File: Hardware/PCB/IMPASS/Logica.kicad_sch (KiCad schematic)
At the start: 69 parts, among them J1 PUENTE H, J10 SENSORES, J12 POWER, J7 PUENTE H, J8 SOLENOIDES, J9 PROG, Q25 2N7002, Q26 2N7002, Q27 2N7002, Q28 2N7002, Q29 2N7002, Q30 2N7002, Q31 2N7002, Q32 2N7002, Q33 2N7002, Q34 2N7002, Q35 2N7002, Q36 2N7002, Q37 2N7002, Q38 2N7002, Q39 2N7002, Q40 2N7002, Q41 2N7002, Q42 2N7002, Q46 2N7002, Q47 2N7002, Q48 2N7002, SW1 RESET, SW2 BOOT, U1 ESP32-S3-WROOM-1, U10 AMS1117-3.3, U11 AMS1117-5.0

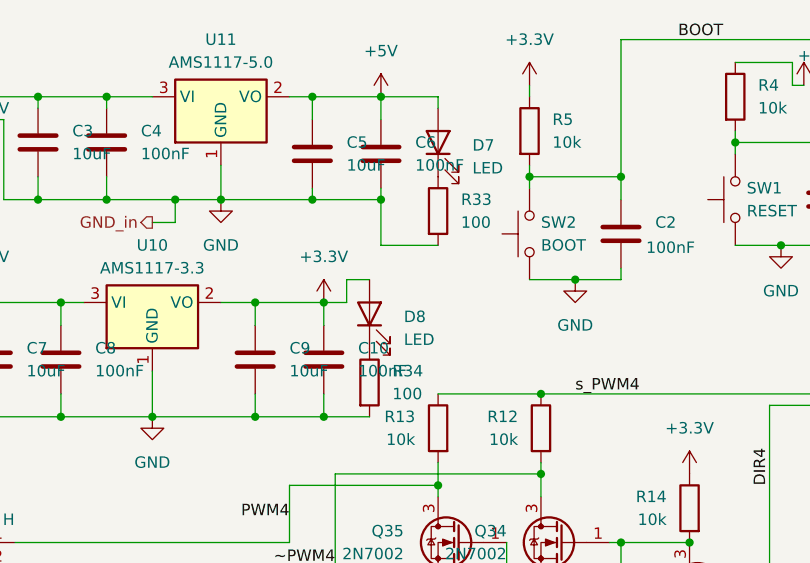
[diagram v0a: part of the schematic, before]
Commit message: Schematics: Added mpu6050
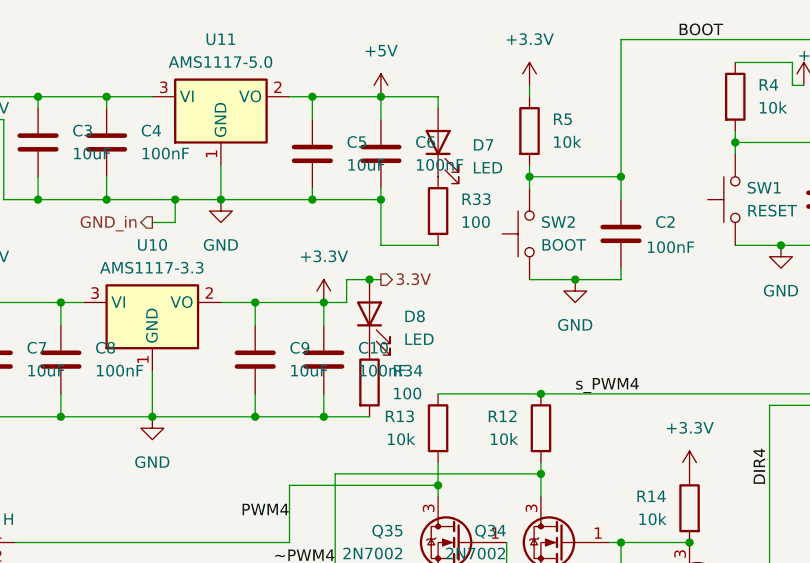
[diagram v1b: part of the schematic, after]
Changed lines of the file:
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@@
 	)
 	(junction
+		(at 63.5 40.64)
+		(diameter 0)
+		(color 0 0 0 0)
+	)
+	(junction
 		(at 204.47 73.66)
 		(diameter 0)
@@
 	(wire
 		(pts
+			(xy 63.5 40.64) (xy 64.77 40.64)
+		)
+		(stroke
+			(width 0)
+			(type default)
+		)
+	)
+	(wire
+		(pts
 			(xy 170.18 30.48) (xy 170.18 36.83)
 		)
@@
 		)
 	)
+	(hierarchical_label "3.3V"
+		(shape output)
+		(at 64.77 40.64 0)
+		(effects
+			(font
+				(size 1.27 1.27)
+			)
+			(justify left)
+		)
+	)

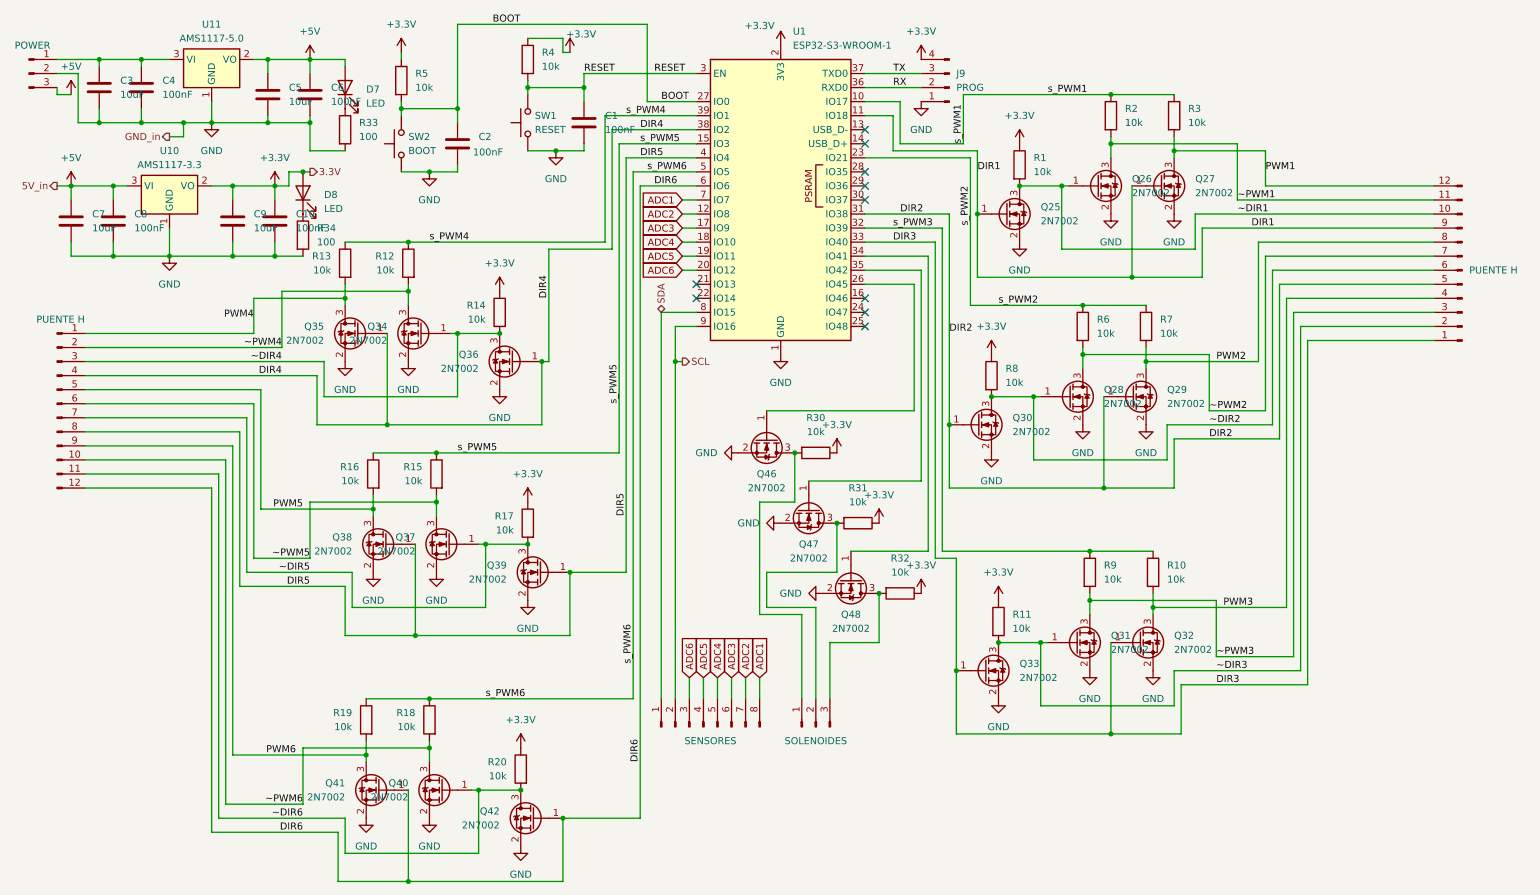
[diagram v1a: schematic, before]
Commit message: Restore all the schematics
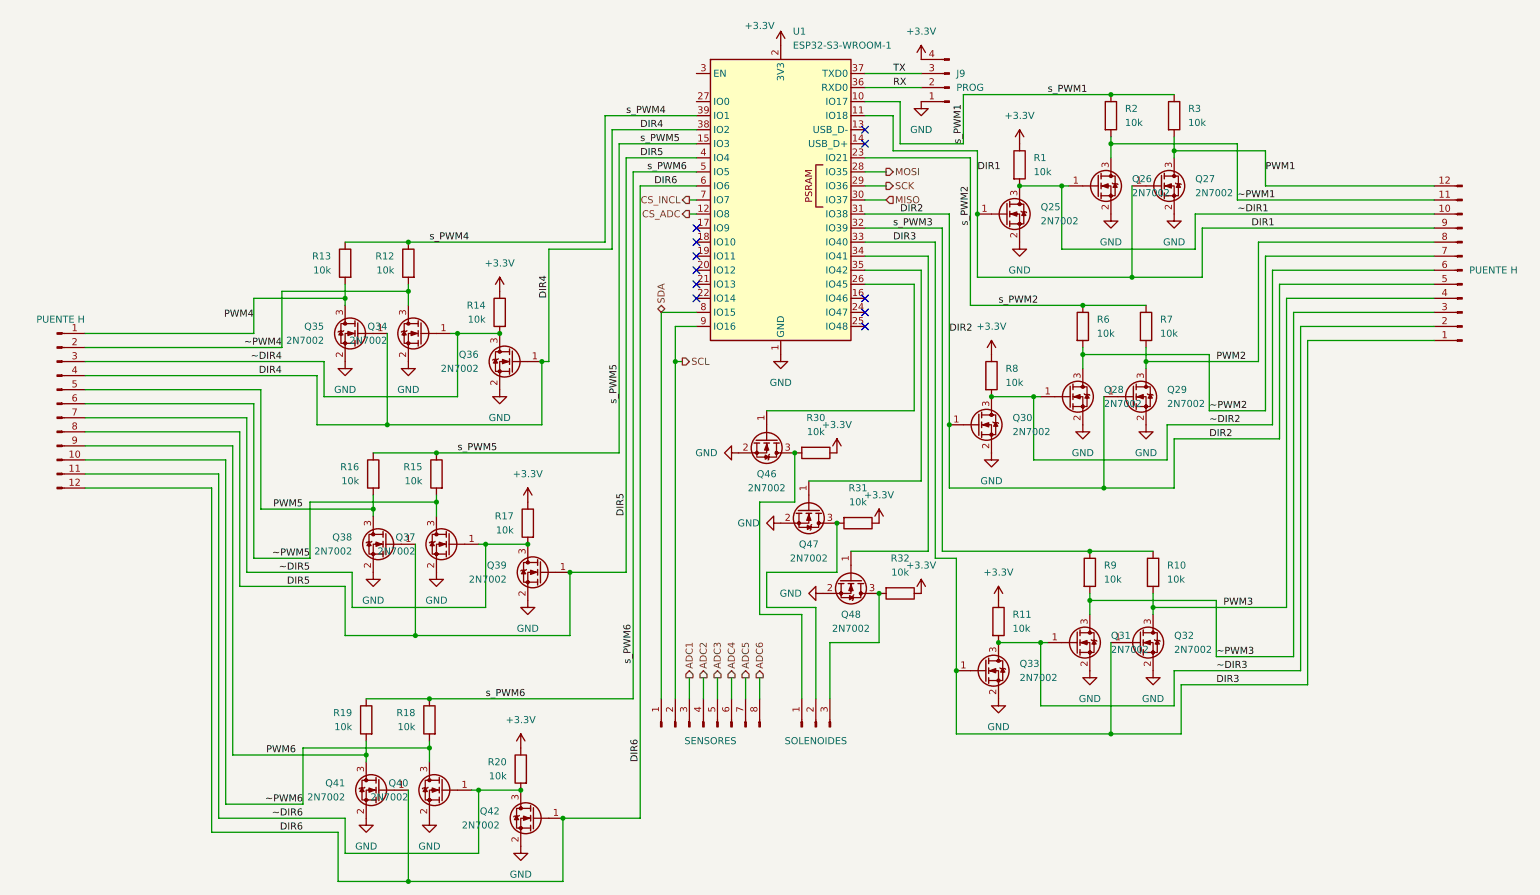
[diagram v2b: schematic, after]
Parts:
- removed C1, C10, C2, C4, C6, C8: 100nF, Capacitor_SMD:C_0603_1608Metric, symbol Device:C
- removed C3, C5, C7, C9: 10uF, Capacitor_SMD:C_0805_2012Metric, symbol Device:C
- removed D7, D8: LED, LED_SMD:LED_0603_1608Metric, symbol Device:LED
- removed J12: POWER, Connector_PinHeader_2.54mm:PinHeader_1x03_P2.54mm_Vertical, symbol Connector:Conn_01x03_Pin
- removed R33, R34: 100, Resistor_SMD:R_0603_1608Metric, symbol Device:R
- removed R4, R5: 10k, Resistor_SMD:R_0603_1608Metric, symbol Device:R
- removed SW1: RESET, Button_Switch_THT:SW_PUSH_6mm_H5mm, symbol Switch:SW_Push
- removed SW2: BOOT, Button_Switch_THT:SW_PUSH_6mm_H5mm, symbol Switch:SW_Push
- removed U10: AMS1117-3.3, Package_TO_SOT_SMD:SOT-223-3_TabPin2, symbol Regulator_Linear:AMS1117-3.3
- removed U11: AMS1117-5.0, Package_TO_SOT_SMD:SOT-223-3_TabPin2, symbol Regulator_Linear:AMS1117-5.0
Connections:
- net ADC1: now also J10.3 (Pin_3); no longer J10.8 (Pin_8), U1.7 (IO7)
- net ADC2: now also J10.4 (Pin_4); no longer J10.7 (Pin_7), U1.12 (IO8)
- net ADC3: now also J10.5 (Pin_5); no longer J10.6 (Pin_6), U1.17 (IO9)
- net ADC4: now also J10.6 (Pin_6); no longer J10.5 (Pin_5), U1.18 (IO10)
- net ADC5: now also J10.7 (Pin_7); no longer J10.4 (Pin_4), U1.19 (IO11)
- net ADC6: now also J10.8 (Pin_8); no longer J10.3 (Pin_3), U1.20 (IO12)
- net MOSI: now reaches U1.28 (IO35)
- net SCK: now reaches U1.29 (IO36)
- net MISO: now reaches U1.30 (IO37)
- net BOOT: no longer names the net of U1.27 (IO0)
- net RESET: no longer names the net of U1.3 (EN)
- new net CS_ADC: U1.12 (IO8)
- new net CS_INCL: U1.7 (IO7)
- no-connect marks 10 -> 11
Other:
- company: (none) -> Luis Miguel Carmona Cortés
- title: (none) -> IMPASS 
